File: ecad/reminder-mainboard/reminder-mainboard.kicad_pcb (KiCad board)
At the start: 2 copper layers, 63.5 x 31.8 mm, 27 parts, among them J1 USB_B_Micro, J2 MOLEX SL 1x5, J3 Conn_01x03_Male, J4 22-03-5065, Q1 2N3904, SW1 SW_SPDT, SW2 SW_Push, SW3 SW_Push, U1 LM1117-3.3, U2 QRD1113GR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

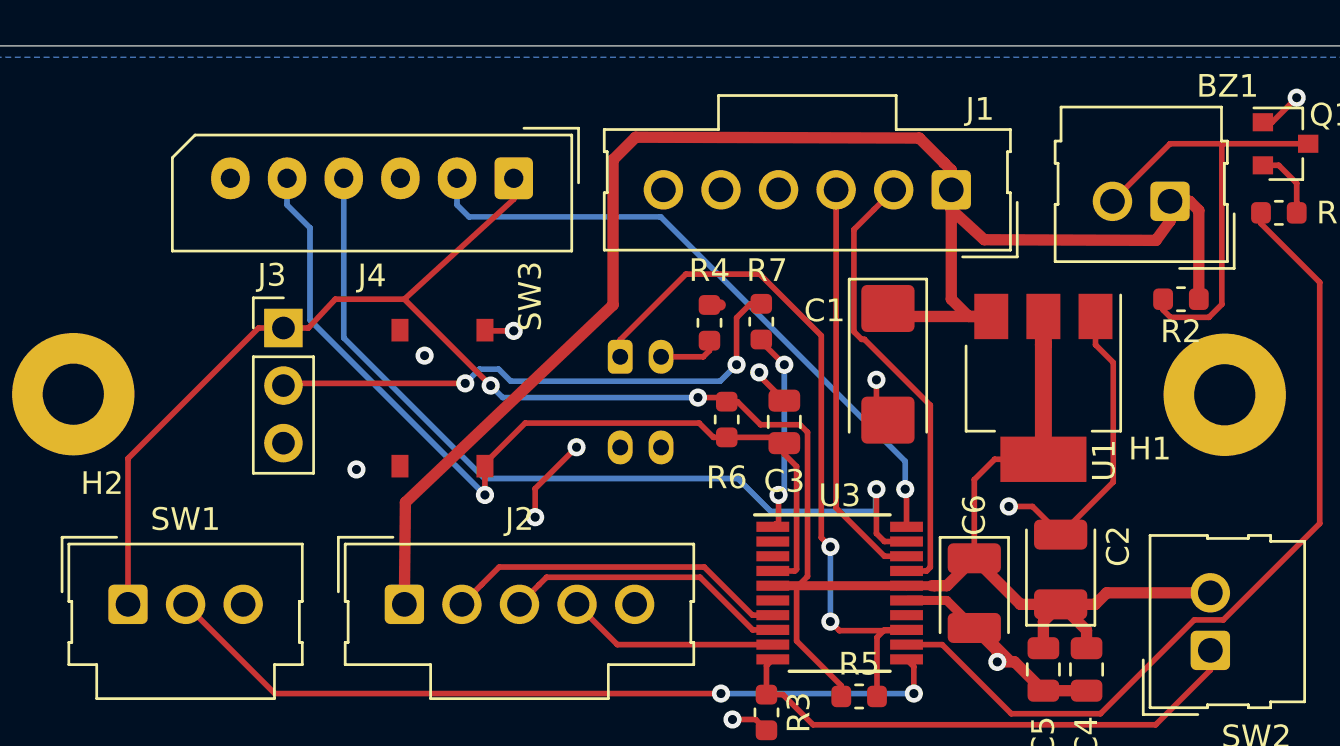
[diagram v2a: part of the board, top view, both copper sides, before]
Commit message: Readied for adding separate usb chip
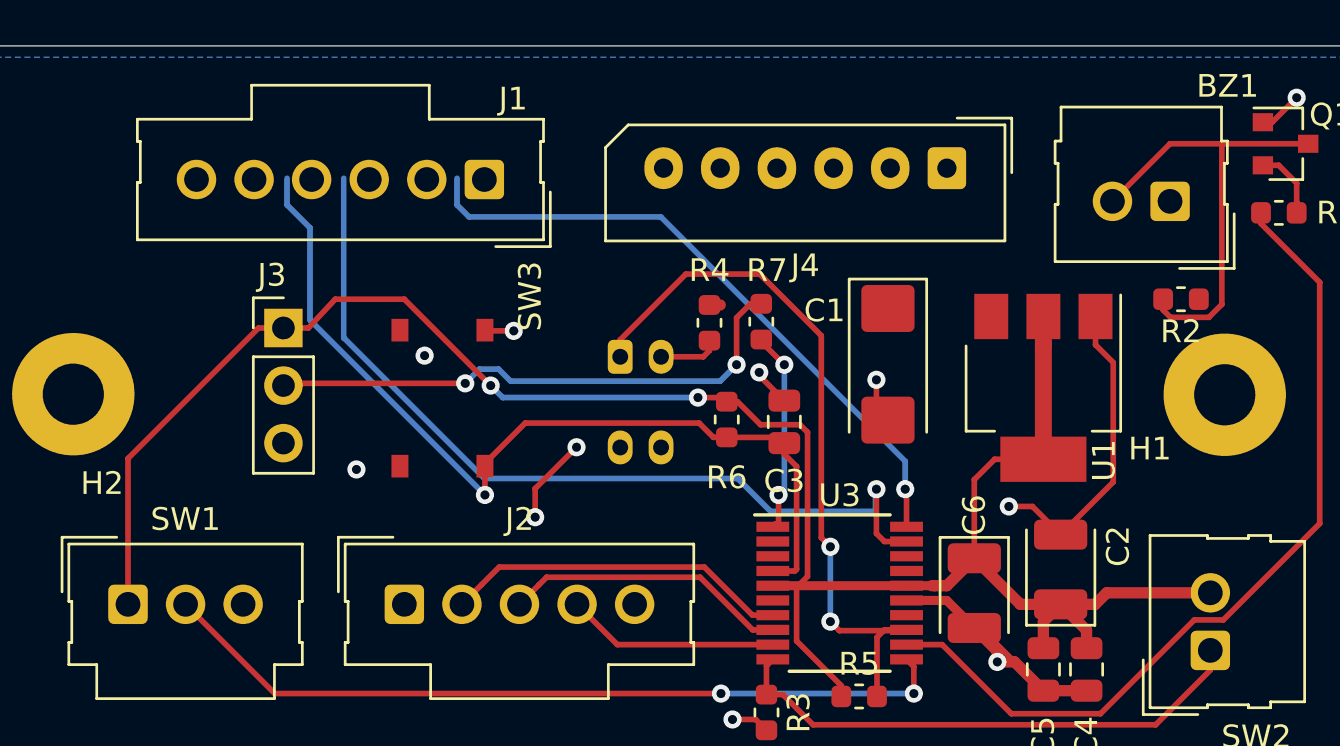
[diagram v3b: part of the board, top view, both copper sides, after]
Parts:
- moved J1 20.6 mm to (88.1, 101.1)
- moved J4 19.1 mm to (108.5, 100.6)
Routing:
- net +5V: track 70.1 -> 0.48 mm
- net /USB_M: track 20.0 -> 0.00 mm
- net /USB_P: track 18.0 -> 0.00 mm
- net +3V3: track 101.8 -> 94.4 mm
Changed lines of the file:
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@@
     (thickness 1.6)
     (drawings 4)
-    (tracks 243)
+    (tracks 207)
     (zones 0)
     (modules 27)
@@
   (layers
     (0 F.Cu signal)
-    (31 B.Cu signal)
+    (31 B.Cu signal hide)
     (32 B.Adhes user)
     (33 F.Adhes user)
@@
   )
   (module Connector_Molex:Molex_SPOX_5267-06A_1x06_P2.50mm_Vertical (layer F.Cu)
-    (at 89.408 101.092 180)
+    (at 108.51962 100.64496 180)
     (descr "Molex SPOX Connector System, 5267-06A, 6 Pins per row (http://www.molex.com/pdm_docs/sd/022035035_sd.pdf), generated with kicad-footprint-generator")
     (tags "connector Molex SPOX side entry")
@@
   )
   (module Connector_Molex:Molex_SL_171971-0006_1x06_P2.54mm_Vertical (layer F.Cu)
-    (at 108.712 101.6 180)
+    (at 88.1126 101.14534 180)
     (descr "Molex Stackable Linear Connector, 171971-0006 (compatible alternatives: 171971-0106, 171971-0206), 6 Pins per row (https://www.molex.com/pdm_docs/sd/1719710002_sd.pdf), generated with kicad-footprint-generator")
     (tags "connector Molex SL vertical")
@@
   (gr_line (start 127 127) (end 127 95.25) (layer Edge.Cuts) (width 0.05))
   (gr_line (start 63.5 127) (end 127 127) (layer Edge.Cuts) (width 0.05))
-  (via (at 90.35288 116.04244) (size 0.8) (drill 0.4) (layers F.Cu B.Cu) (net 3))
-  (via (at 92.17914 112.95634) (size 0.8) (drill 0.4) (layers F.Cu B.Cu) (net 3))
-  (segment (start 90.35288 114.7826) (end 92.17914 112.95634) (width 0.25) (layer F.Cu) (net 3))
-  (segment (start 90.35288 116.04244) (end 90.35288 114.7826) (width 0.25) (layer F.Cu) (net 3))
   (segment (start 118.364 99.568) (end 115.824 102.108) (width 0.25) (layer F.Cu) (net 1))
   (segment (start 120.077984 107.22601) (end 120.65 106.653994) (width 0.25) (layer F.Cu) (net 1))
@@
   (segment (start 120.65 99.568) (end 118.364 99.568) (width 0.25) (layer F.Cu) (net 1))
   (segment (start 124.46 99.568) (end 120.65 99.568) (width 0.25) (layer F.Cu) (net 1))
-  (segment (start 119.234 102.108) (end 118.364 102.108) (width 0.5) (layer F.Cu) (net 2))
-  (segment (start 119.634 102.508) (end 119.234 102.108) (width 0.5) (layer F.Cu) (net 2))
-  (segment (start 119.634 106.426) (end 119.634 102.508) (width 0.5) (layer F.Cu) (net 2))
-  (segment (start 106.271 107.188) (end 105.918 106.835) (width 0.5) (layer F.Cu) (net 2))
-  (segment (start 110.476 107.188) (end 106.271 107.188) (width 0.5) (layer F.Cu) (net 2))
-  (segment (start 109.476 107.188) (end 110.476 107.188) (width 0.5) (layer F.Cu) (net 2))
-  (segment (start 108.712 106.424) (end 109.476 107.188) (width 0.5) (layer F.Cu) (net 2))
-  (segment (start 108.712 101.6) (end 108.712 106.424) (width 0.5) (layer F.Cu) (net 2))
   (segment (start 98.519 106.68) (end 98.044 106.68) (width 0.5) (layer F.Cu) (net 2))
-  (segment (start 108.712 102.47) (end 108.712 101.6) (width 0.5) (layer F.Cu) (net 2))
-  (segment (start 110.16742 103.80218) (end 108.712 102.47) (width 0.5) (layer F.Cu) (net 2))
-  (segment (start 117.74424 103.83012) (end 110.16742 103.80218) (width 0.5) (layer F.Cu) (net 2))
-  (segment (start 118.364 102.978) (end 117.74424 103.83012) (width 0.5) (layer F.Cu) (net 2))
-  (segment (start 118.364 102.108) (end 118.364 102.978) (width 0.5) (layer F.Cu) (net 2))
-  (segment (start 108.712 100.73) (end 108.712 101.6) (width 0.5) (layer F.Cu) (net 2))
-  (segment (start 108.390759 100.404999) (end 108.386999 100.404999) (width 0.5) (layer F.Cu) (net 2))
-  (segment (start 107.3023 99.31654) (end 108.390759 100.404999) (width 0.5) (layer F.Cu) (net 2))
-  (segment (start 94.78772 99.27844) (end 107.3023 99.31654) (width 0.5) (layer F.Cu) (net 2))
-  (segment (start 108.386999 100.404999) (end 108.712 100.73) (width 0.5) (layer F.Cu) (net 2))
-  (segment (start 93.789998 100.276162) (end 94.78772 99.27844) (width 0.5) (layer F.Cu) (net 2))
-  (segment (start 93.789998 106.68) (end 93.789998 100.276162) (width 0.5) (layer F.Cu) (net 2))
-  (segment (start 84.62772 115.38966) (end 93.789998 106.68) (width 0.5) (layer F.Cu) (net 2))
-  (segment (start 84.582 119.888) (end 84.62772 115.38966) (width 0.5) (layer F.Cu) (net 2))
+  (via (at 90.35288 116.04244) (size 0.8) (drill 0.4) (layers F.Cu B.Cu) (net 3))
+  (via (at 92.17914 112.95634) (size 0.8) (drill 0.4) (layers F.Cu B.Cu) (net 3))
+  (segment (start 90.35288 114.7826) (end 92.17914 112.95634) (width 0.25) (layer F.Cu) (net 3))
+  (segment (start 90.35288 116.04244) (end 90.35288 114.7826) (width 0.25) (layer F.Cu) (net 3))
   (segment (start 115.076 108.438) (end 115.858 109.22) (width 0.25) (layer F.Cu) (net 3))
   (segment (start 115.076 107.188) (end 115.076 108.438) (width 0.25) (layer F.Cu) (net 3))
@@
   (segment (start 81.534 106.426) (end 80.348 107.696) (width 0.25) (layer F.Cu) (net 4))
   (segment (start 84.582 106.426) (end 81.534 106.426) (width 0.25) (layer F.Cu) (net 4))
-  (segment (start 89.408 102.017) (end 84.582 106.426) (width 0.25) (layer F.Cu) (net 4))
-  (segment (start 89.408 101.092) (end 89.408 102.017) (width 0.25) (layer F.Cu) (net 4))
   (via (at 88.392 110.236) (size 0.8) (drill 0.4) (layers F.Cu B.Cu) (net 4))
   (segment (start 84.582 106.426) (end 88.392 110.236) (width 0.25) (layer F.Cu) (net 4))
@@
   (segment (start 98.218988 112.522) (end 97.587978 111.89099) (width 0.25) (layer F.Cu) (net 5))
   (segment (start 98.806 112.522) (end 98.218988 112.522) (width 0.25) (layer F.Cu) (net 5))
-  (segment (start 105.763 117.766) (end 106.738 117.766) (width 0.25) (layer F.Cu) (net 6))
-  (segment (start 103.632 115.635) (end 105.763 117.766) (width 0.25) (layer F.Cu) (net 6))
-  (segment (start 103.632 101.6) (end 103.632 115.635) (width 0.25) (layer F.Cu) (net 6))
-  (segment (start 104.41799 103.35401) (end 105.302001 102.469999) (width 0.25) (layer F.Cu) (net 7))
-  (segment (start 104.41799 107.86068) (end 104.41799 103.35401) (width 0.25) (layer F.Cu) (net 7))
-  (segment (start 104.75482 108.19751) (end 104.41799 107.86068) (width 0.25) (layer F.Cu) (net 7))
-  (segment (start 104.8812 108.19751) (end 104.75482 108.19751) (width 0.25) (layer F.Cu) (net 7))
-  (segment (start 107.788001 111.104311) (end 104.8812 108.19751) (width 0.25) (layer F.Cu) (net 7))
-  (segment (start 105.302001 102.469999) (end 106.172 101.6) (width 0.25) (layer F.Cu) (net 7))
-  (segment (start 107.788001 118.251001) (end 107.788001 111.104311) (width 0.25) (layer F.Cu) (net 7))
-  (segment (start 107.623002 118.416) (end 107.788001 118.251001) (width 0.25) (layer F.Cu) (net 7))
-  (segment (start 106.738 118.416) (end 107.623002 118.416) (width 0.25) (layer F.Cu) (net 7))
   (via (at 98.552 123.825) (size 0.8) (drill 0.4) (layers F.Cu B.Cu) (net 8))
   (segment (start 78.867 123.825) (end 98.552 123.825) (width 0.25) (layer F.Cu) (net 8))

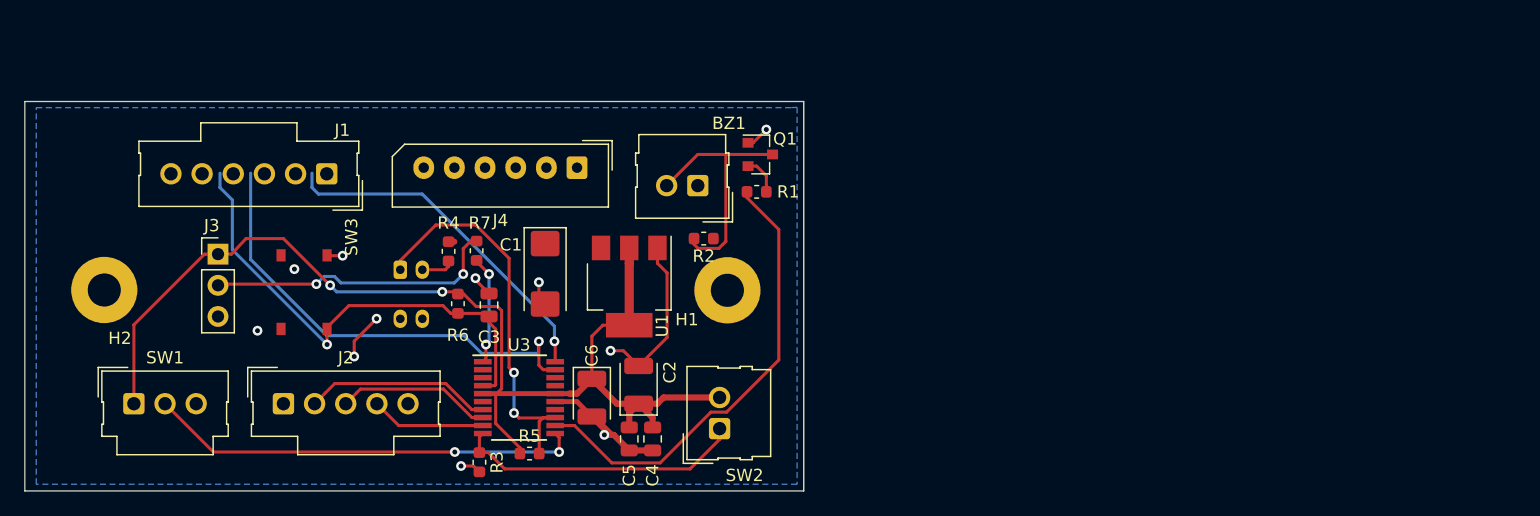
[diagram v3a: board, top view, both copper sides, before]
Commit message: Finished mainboard pcb routing
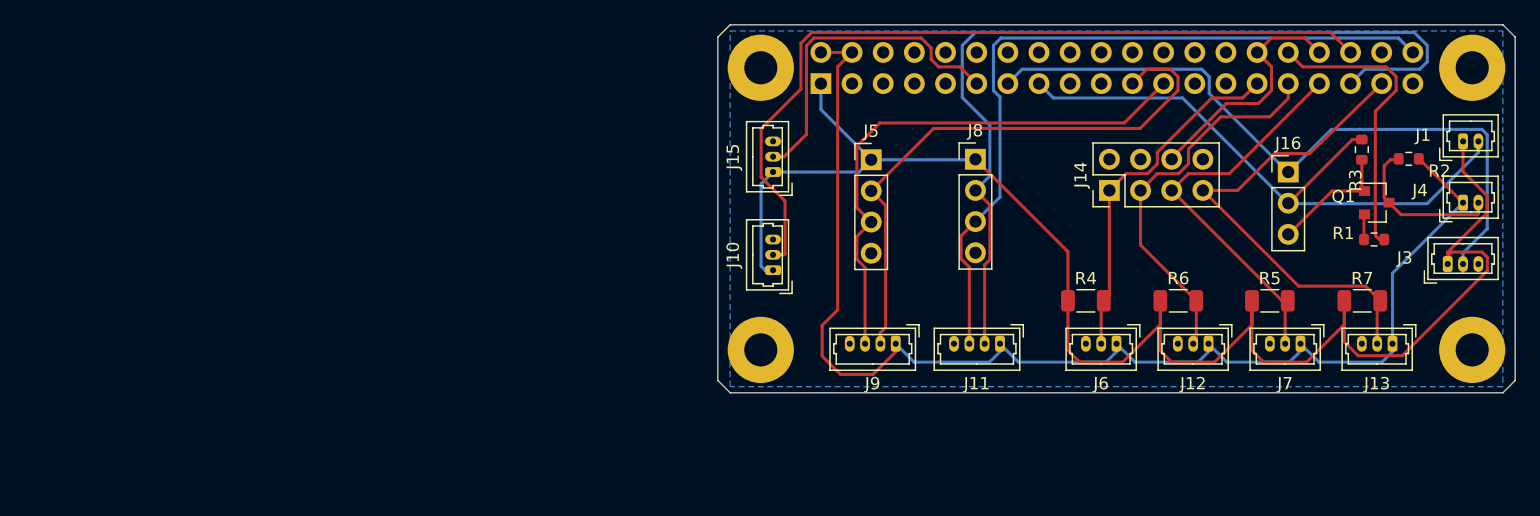
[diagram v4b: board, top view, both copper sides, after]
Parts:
- removed BZ1: Buzzer, Connector_Molex:Molex_SL_171971-0002_1x02_P2.54mm_Vertical
- removed C1: 10uF, Capacitor_Tantalum_SMD:CP_EIA-6032-28_Kemet-C
- removed C2: 100uF, Capacitor_Tantalum_SMD:CP_EIA-3528-21_Kemet-B
- removed C3, C4, C5: 100nF, Capacitor_SMD:C_0805_2012Metric
- removed C6: 10uF, Capacitor_Tantalum_SMD:CP_EIA-3528-21_Kemet-B
- removed J2: MOLEX SL 1x5, Connector_Molex:Molex_SL_171971-0005_1x05_P2.54mm_Vertical
- removed SW1: SW_SPDT, Connector_Molex:Molex_SL_171971-0003_1x03_P2.54mm_Vertical
- removed SW2: SW_Push, Connector_Molex:Molex_SL_171971-0002_1x02_P2.54mm_Vertical
- removed SW3: SW_Push, jlcpcb:TACT_SWITCH_TS-1187A-X-X-X
- removed U1: LM1117-3.3, Package_TO_SOT_SMD:SOT-223-3_TabPin2
- removed U2: QRD1113GR, OptoDevice:Everlight_ITR8307F43
- removed U3: STM32F042F4Px, Package_SO:TSSOP-20_4.4x6.5mm_P0.65mm
- added H3: MountingHole, MountingHole:MountingHole_2.7mm_M2.5_Pad, F.Cu at (123.5, 115.5)
- added H4: MountingHole, MountingHole:MountingHole_2.7mm_M2.5_Pad, F.Cu at (181.5, 92.5)
- added J10: 0530470310, Connector_Molex:Molex_PicoBlade_53047-0310_1x03_P1.25mm_Vertical, F.Cu at (124.5, 109.0)
- added J11: 0530470410, Connector_Molex:Molex_PicoBlade_53047-0410_1x04_P1.25mm_Vertical, F.Cu at (143.0, 115.0)
- added J12: 0530470310, Connector_Molex:Molex_PicoBlade_53047-0310_1x03_P1.25mm_Vertical, F.Cu at (160.0, 115.0)
- added J13: 0530470310, Connector_Molex:Molex_PicoBlade_53047-0310_1x03_P1.25mm_Vertical, F.Cu at (175.0, 115.0)
- added J14: Conn_02x04_Odd_Even, Connector_PinHeader_2.54mm:PinHeader_2x04_P2.54mm_Vertical, F.Cu at (151.9, 102.5)
- added J15: 0530470310, Connector_Molex:Molex_PicoBlade_53047-0310_1x03_P1.25mm_Vertical, F.Cu at (124.5, 101.0)
- added J16: Conn_01x03_Male, Connector_PinHeader_2.54mm:PinHeader_1x03_P2.54mm_Vertical, F.Cu at (166.5, 101.0)
- added J17: Raspberry_Pi_2_3, Connector_PinSocket_2.54mm:PinSocket_2x20_P2.54mm_Vertical, B.Cu at (128.4, 93.8)
- added J5: Conn_01x04_Male, Connector_PinHeader_2.54mm:PinHeader_1x04_P2.54mm_Vertical, F.Cu at (132.5, 100.0)
- added J6: 0530470310, Connector_Molex:Molex_PicoBlade_53047-0310_1x03_P1.25mm_Vertical, F.Cu at (152.5, 115.0)
- added J7: 0530470310, Connector_Molex:Molex_PicoBlade_53047-0310_1x03_P1.25mm_Vertical, F.Cu at (167.5, 115.0)
- added J8: Conn_01x04_Male, Connector_PinHeader_2.54mm:PinHeader_1x04_P2.54mm_Vertical, F.Cu at (141.0, 100.0)
- added J9: 0530470410, Connector_Molex:Molex_PicoBlade_53047-0410_1x04_P1.25mm_Vertical, F.Cu at (134.5, 115.0)
- J1: value USB_B_Micro -> 0530470210; footprint Connector_Molex:Molex_SL_171971-0006_1x06_P2.54mm_Vertical -> Connector_Molex:Molex_PicoBlade_53047-0210_1x02_P1.25mm_Vertical
- J3: value Conn_01x03_Male -> 0530470310; footprint Connector_PinHeader_2.54mm:PinHeader_1x03_P2.54mm_Vertical -> Connector_Molex:Molex_PicoBlade_53047-0310_1x03_P1.25mm_Vertical
- J4: value 22-03-5065 -> 0530470210; footprint Connector_Molex:Molex_SPOX_5267-06A_1x06_P2.50mm_Vertical -> Connector_Molex:Molex_PicoBlade_53047-0210_1x02_P1.25mm_Vertical
- R4: value 160 -> 15k; footprint Resistor_SMD:R_0603_1608Metric -> Resistor_SMD:R_1206_3216Metric
- R5, R6, R7: value 10k -> 15k; footprint Resistor_SMD:R_0603_1608Metric -> Resistor_SMD:R_1206_3216Metric
- moved J3 100.3 mm to (179.5, 108.5)
- moved J1 92.7 mm to (180.8, 98.5), turned to 0 degrees
- moved R3 76.3 mm to (172.5, 99.2)
- moved R7 72.3 mm to (172.5, 111.5), turned to 0 degrees
- moved J4 72.3 mm to (180.8, 103.5), turned to 0 degrees
- moved R5 61.6 mm to (165.0, 111.5)
- moved H1 60.9 mm to (181.5, 115.5)
- moved R6 58.7 mm to (157.5, 111.5), turned to 0 degrees
- moved R2 57.8 mm to (176.3, 99.9)
- moved H2 56.5 mm to (123.5, 92.5)
- moved R4 52.1 mm to (150.0, 111.5), turned to 0 degrees
- moved R1 50.5 mm to (173.5, 106.5), turned to 180 degrees
- moved Q1 50.4 mm to (173.7, 103.5)
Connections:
- J1 pad 1: +5V -> +3V3
- J1 pad 2: /USB_M -> /UI_BUTTON
- J3 pad 2: Net-(J3-Pad2) -> /MUTE
- J4 pad 1: +3V3 -> +5V
- J4 pad 2: /SWCLK -> Net-(J4-Pad2)
- Q1 pad 3: Net-(BZ1-Pad2) -> Net-(J4-Pad2)
- R2 pad 2: Net-(BZ1-Pad2) -> Net-(J4-Pad2)
- R4 pad 1: +5V -> +3V3
- R4 pad 2: Net-(R4-Pad2) -> /PROX1_OUT
- R5 pad 2: /SENSOR -> /PROX3_OUT
- R6 pad 2: /NRST -> /PROX2_OUT
- R7 pad 1: Net-(R7-Pad1) -> +3V3
- R7 pad 2: Net-(J3-Pad2) -> /PROX4_OUT
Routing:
- net +5V: track 0.48 -> 104.1 mm
- net /LED1_SDO: track 0.00 -> 73.5 mm
- net /EXP0: track 0.00 -> 66.2 mm
- net /LED1_SCK: track 0.00 -> 61.1 mm
- net /LED0_SDO: track 0.00 -> 47.1 mm
- net /LED0_SCK: track 0.00 -> 44.5 mm
- net /NRST: track 40.2 -> 0.00 mm, vias 1 -> 0
- net /PROX4_OUT: track 0.00 -> 39.9 mm
- net /SWDIO: track 38.1 -> 0.00 mm, vias 1 -> 0
- net +3V3: track 94.4 -> 130.0 mm, vias 2 -> 0
- net /PROX3_OUT: track 0.00 -> 32.4 mm
- net /SENSOR: track 32.3 -> 0.00 mm, vias 2 -> 0
- net /PROX2_OUT: track 0.00 -> 31.7 mm
- net /PROX1_OUT: track 0.00 -> 29.0 mm
- net /SWCLK: track 28.5 -> 0.00 mm, vias 1 -> 0
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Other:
- board size 63.5 x 31.8 mm -> 65 x 30 mm

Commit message: PCB routing changes
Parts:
- removed J11, J9: 0530470410, Connector_Molex:Molex_PicoBlade_53047-0410_1x04_P1.25mm_Vertical
- J5, J8: value Conn_01x04_Male -> Conn_01x03_Male; footprint Connector_PinHeader_2.54mm:PinHeader_1x04_P2.54mm_Vertical -> Connector_PinHeader_2.54mm:PinHeader_1x03_P2.54mm_Vertical
- moved J5 60.5 mm to (190.9, 115.9)
- moved J8 60.5 mm to (199.4, 115.8)
- moved J14 53.2 mm to (187.3, 142.2)
- moved J1 31.1 mm to (211.9, 98.5)
- moved J3 31.1 mm to (210.6, 108.5)
- moved J4 31.1 mm to (211.9, 103.5)
- moved Q1 31.1 mm to (204.8, 103.5)
- moved R1 31.1 mm to (204.6, 106.5)
- moved R2 31.1 mm to (207.4, 99.9)
- moved R3 31.1 mm to (203.6, 99.2)
- moved J16 28.5 mm to (172.1, 128.9)
- moved J6 18.5 mm to (134.0, 114.3)
- moved R4 17.7 mm to (132.7, 107.8), turned to 270 degrees
- moved J12 17.2 mm to (142.9, 114.3)
- moved R6 16.4 mm to (141.6, 107.8), turned to 270 degrees
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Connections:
- J12 pad 2: /PROX2_OUT -> /PROX1_OUT
- J13 pad 2: /PROX4_OUT -> /PROX3_OUT
- J14 pad 1: /PROX1_OUT -> /PROX0_OUT
- J14 pad 3: /PROX2_OUT -> /PROX1_OUT
- J14 pad 5: /PROX3_OUT -> /PROX2_OUT
- J14 pad 7: /PROX4_OUT -> /PROX3_OUT
- J17 pad 10: (no net) -> /EXP0
- J17 pad 11: /EXP1 -> /PROX1_OUT
- J17 pad 13: /MUTE -> /PROX2_OUT
- J17 pad 14: (no net) -> GND
- J17 pad 15: /UI_BUTTON -> /PROX3_OUT
- J17 pad 17: (no net) -> +3V3
- J17 pad 20: (no net) -> GND
- J17 pad 25: (no net) -> GND
- J17 pad 29: /PROX1_OUT -> /UI_BUTTON
- J17 pad 31: /PROX2_OUT -> /MUTE
- J17 pad 32: /BUZZER -> (no net)
- J17 pad 33: /PROX3_OUT -> /BUZZER
- J17 pad 36: /EXP0 -> (no net)
- J17 pad 37: /PROX4_OUT -> (no net)
- J17 pad 39: (no net) -> GND
- J17 pad 7: (no net) -> /PROX0_OUT
- J17 pad 8: (no net) -> /EXP1
- J17 pad 9: (no net) -> GND
- J5 pad 1: +3V3 -> /LED0_SDO
- J5 pad 2: /LED0_SDO -> /LED0_SCK
- J5 pad 3: /LED0_SCK -> GND
- J6 pad 2: /PROX1_OUT -> /PROX0_OUT
- J7 pad 2: /PROX3_OUT -> /PROX2_OUT
- J8 pad 1: +3V3 -> /LED1_SDO
- J8 pad 2: /LED1_SDO -> /LED1_SCK
- J8 pad 3: /LED1_SCK -> GND
- R4 pad 2: /PROX1_OUT -> /PROX0_OUT
- R5 pad 2: /PROX3_OUT -> /PROX2_OUT
- R6 pad 2: /PROX2_OUT -> /PROX1_OUT
- R7 pad 2: /PROX4_OUT -> /PROX3_OUT
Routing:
- net +3V3: track 130.0 -> 0.00 mm
- net +5V: track 104.1 -> 0.00 mm
- net /LED1_SDO: track 73.5 -> 0.00 mm
- net /LED1_SCK: track 61.1 -> 0.00 mm
- net /MUTE: track 56.9 -> 0.00 mm
- net /UI_BUTTON: track 50.7 -> 0.00 mm
- net /LED0_SDO: track 47.1 -> 0.00 mm
- net /LED0_SCK: track 44.5 -> 0.00 mm
- net /PROX4_OUT: track 39.9 -> 0.00 mm
- net /EXP0: track 66.2 -> 32.3 mm
- net /PROX3_OUT: track 32.4 -> 0.00 mm
- net /PROX2_OUT: track 31.7 -> 0.00 mm
- net GND: track 30.5 -> 0.00 mm
- net /PROX1_OUT: track 29.0 -> 0.00 mm
- net /BUZZER: track 24.1 -> 0.00 mm
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- removed copper zone on B.Cu, net GND
